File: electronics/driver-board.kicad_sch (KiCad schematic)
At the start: 65 parts, among them J1 Conn_01x02, J3 Motor_Conn_01x04, J5 Conn_01x06_Female, SW1 SW_Push, SW2 SW_Push, U2 LMR16020PDDAR, U3 ESP32-C6-MINI-1/U, U4 AMS1117-3.3, U5 TMC5240-TSSOP38, U6 MT6835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

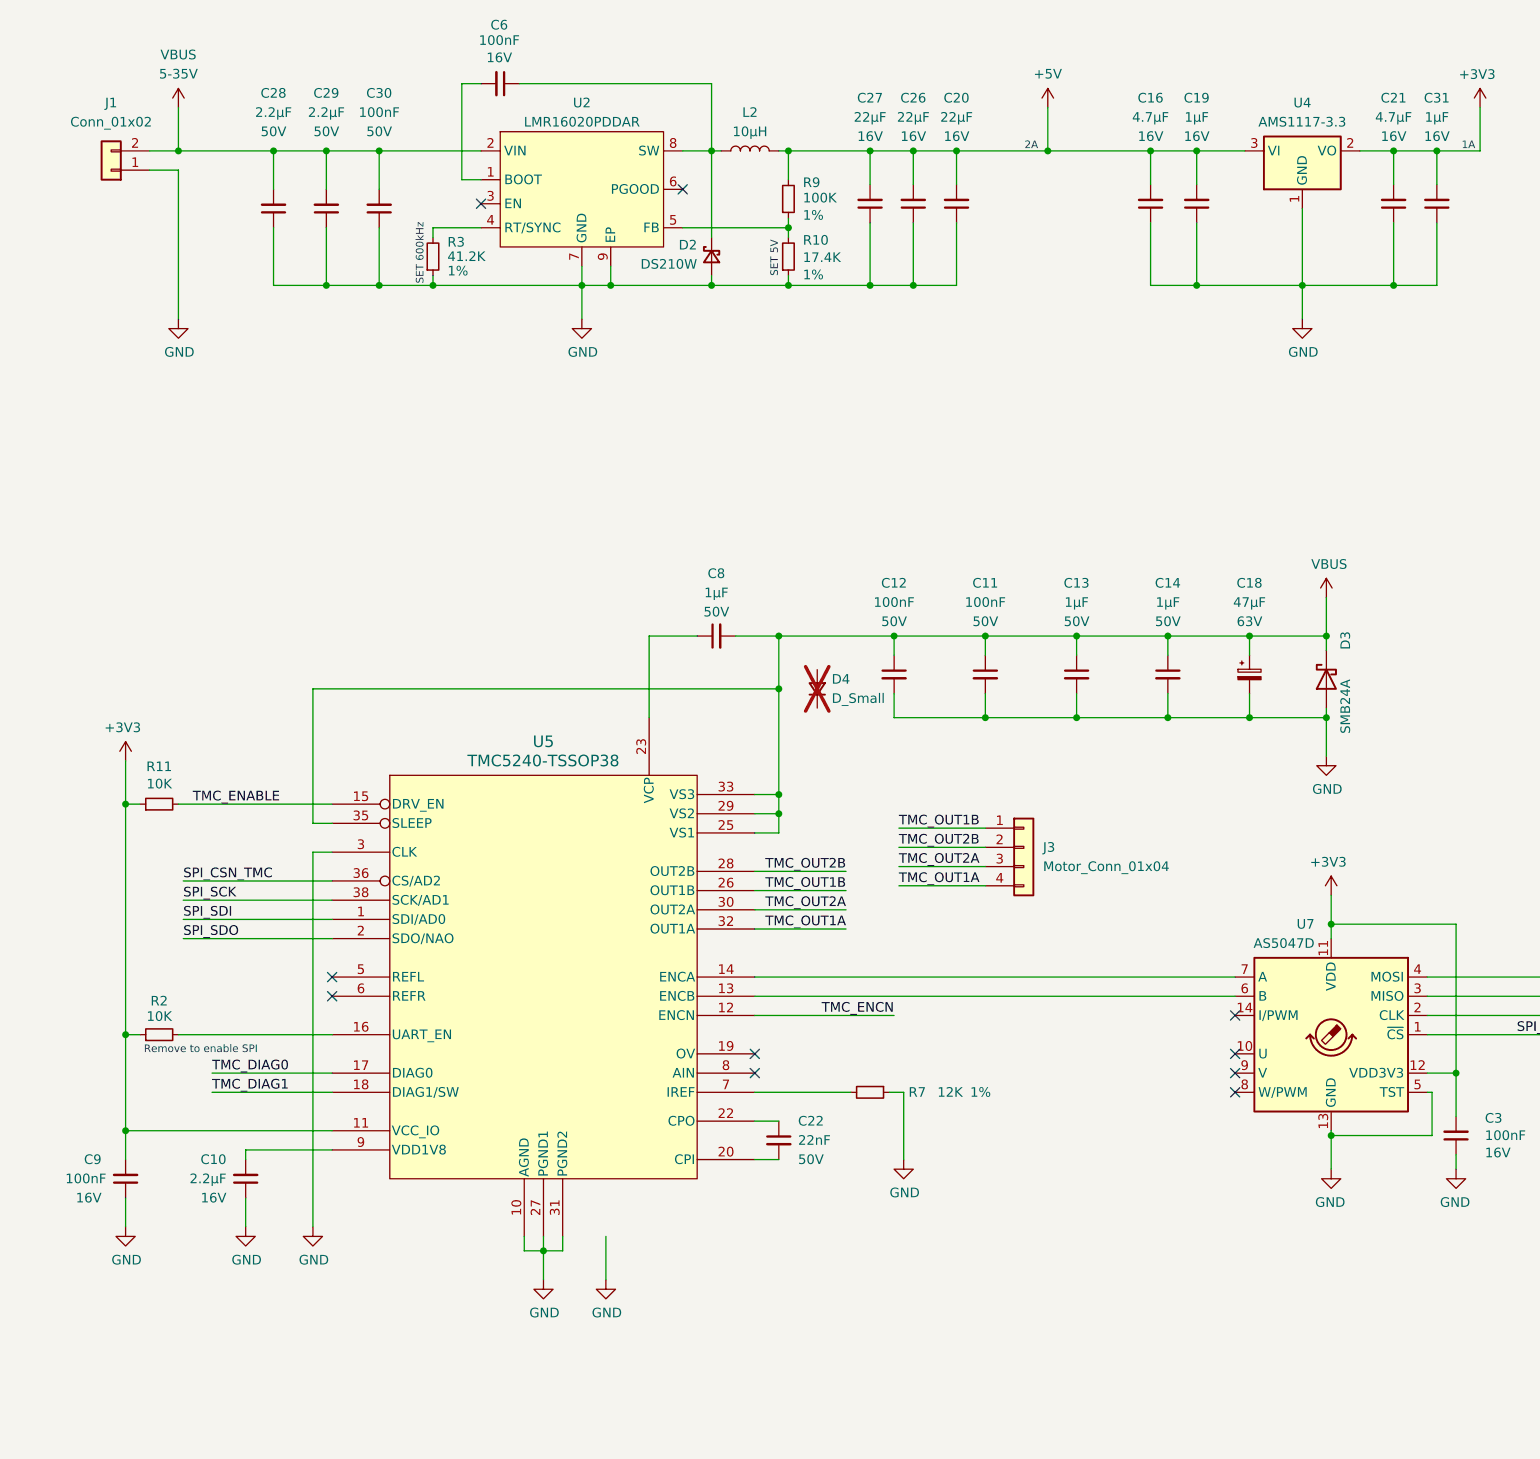
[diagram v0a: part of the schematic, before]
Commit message: splitted power cap into two and changed connector to wago
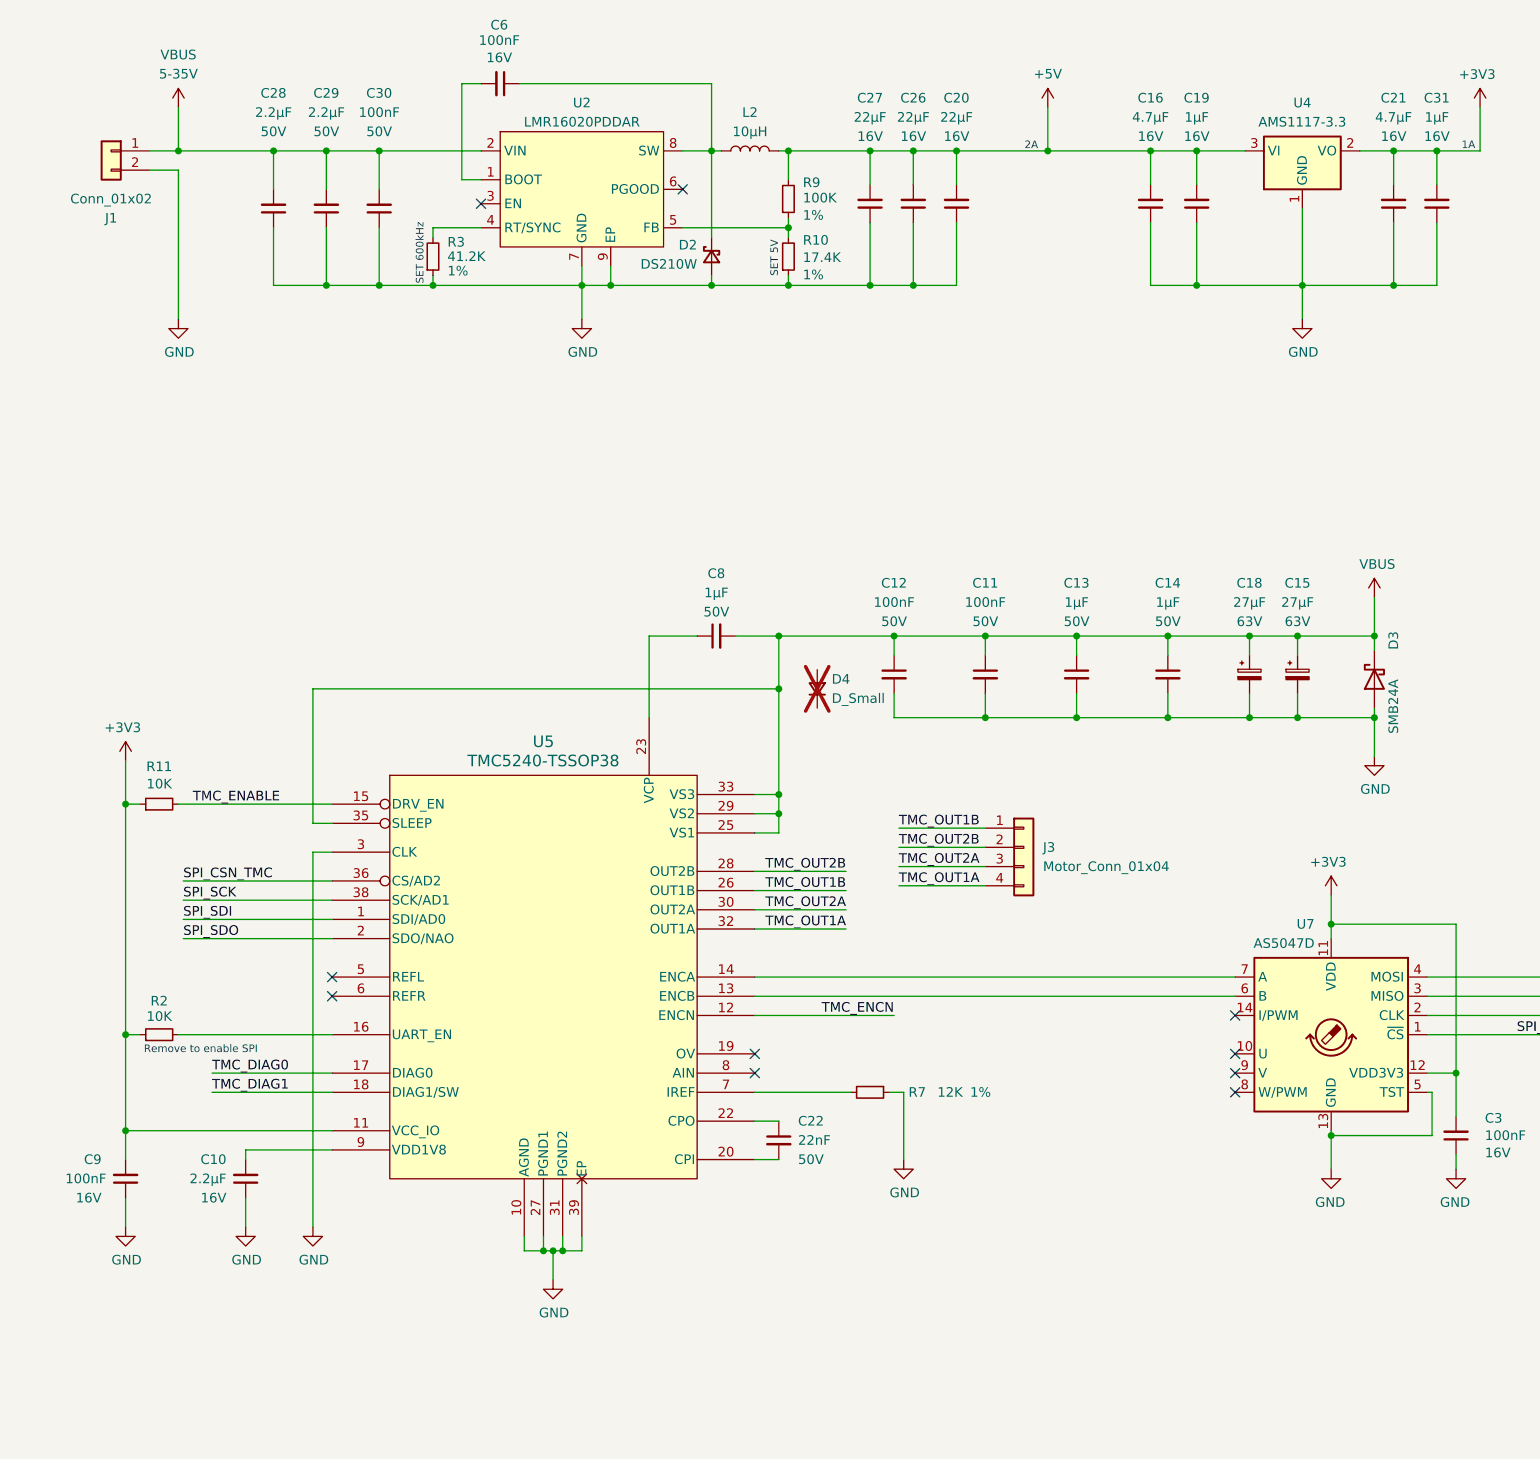
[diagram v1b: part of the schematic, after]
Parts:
- added C15: 27µF, Capacitor_SMD:CP_Elec_5x5.9, symbol Device:C_Polarized_Small
- C1, C17, C3, C4, C6, C9: LCSC (none) -> C66501; Manf# (none) -> CL10B104KO8NNNC; lcsc_part_number C66501 -> (none); mfr_part_number CL10B104KO8NNNC -> (none)
- C10: LCSC (none) -> C23630; Manf# (none) -> CL10A225KO8NNNC; lcsc_part_number C23630 -> (none); mfr_part_number CL10A225KO8NNNC -> (none)
- C11, C12, C30: LCSC (none) -> C1591; Manf# (none) -> CL10B104KB8NNNC; lcsc_part_number C1591 -> (none); mfr_part_number CL10B104KB8NNNC -> (none)
- C13, C14, C8: LCSC (none) -> C15849; Manf# (none) -> CL10A105KB8NNNC; lcsc_part_number C15849 -> (none); mfr_part_number CL10A105KB8NNNC -> (none)
- C16, C21: LCSC (none) -> C19666; Manf# (none) -> CL10A475KO8NNNC; lcsc_part_number C19666 -> (none); mfr_part_number CL10A475KO8NNNC -> (none)
- C18: value 47µF -> 27µF; LCSC (none) -> C487378; Manf (none) -> Ymin; Manf# (none) -> VKMB1001J270MV
- C19, C2, C31, C7: LCSC (none) -> C1592; Manf# (none) -> CL10A105KO8NNNC; lcsc_part_number C1592 -> (none); mfr_part_number CL10A105KO8NNNC -> (none)
- C20, C26, C27: LCSC (none) -> C2762594; Manf# (none) -> CL10A226MO7JZNC; lcsc_part_number C2762594 -> (none); mfr_part_number CL10A226MO7JZNC -> (none)
- C22: LCSC (none) -> C21122; Manf# (none) -> CL10B223KB8NNNC; lcsc_part_number C21122 -> (none); mfr_part_number CL10B223KB8NNNC -> (none)
- C28, C29: LCSC (none) -> C913904; Manf# (none) -> CL10A225KB8NNNC; lcsc_part_number C913904 -> (none); mfr_part_number CL10A225KB8NNNC -> (none)
- C5: LCSC (none) -> C92487; Manf# (none) -> CL10A106MO8NQNC; lcsc_part_number C92487 -> (none); mfr_part_number CL10A106MO8NQNC -> (none)
- D1: LCSC (none) -> C965555; Manf (none) -> Worldsemi; Manf# (none) -> WS2812B-2020; lcsc_part_number C965555 -> (none); mfr_part_number WS2812B-2020 -> (none)
- D2: LCSC (none) -> C116100; Manf (none) -> shikues; Manf# (none) -> DS210W; lcsc_part_number C116100 -> (none); mfr_part_number DS210W -> (none)
- D3: footprint Diode_SMD:D_1210_3225Metric -> Diode_SMD:D_SMB; DigiKey (none) -> F11623TR-ND; LCSC (none) -> C1975909; Manf (none) -> Littelfuse; Manf# (none) -> SZP6SMB24AT3G; digikey_part_number 2156-P6SMB24AT3G-ND -> (none); mfr_part_number P6SMB24AT3G -> (none)
- J1: footprint Connector_TE-Connectivity:TE_2834006-2_1x02_P4.0mm_Horizontal -> Slimc_Connector_Wago:2060-472&slash_998-404; LCSC (none) -> C3310225; Manf (none) -> Wago; Manf# (none) -> 2060-472/998-404; lcsc_part_number C86483 -> (none); mfr_part_number 2834006-2 -> (none)
- J3: DigiKey (none) -> 455-2243-ND; LCSC (none) -> C157925; Manf (none) -> JST; Manf# (none) -> S4B-XH-A; digikey_part_number 455-2243-ND -> (none); lcsc_part_number C157925 -> (none); mfr_part_number S4B-XH-A -> (none)
- L2: LCSC (none) -> C844996; Manf# (none) -> IHLP2020CZER100M01; lcsc_part_number C844996 -> (none); mfr_part_number IHLP2020CZER100M01 -> (none)
- R1, R11, R2, R4: LCSC (none) -> C4226066; Manf# (none) -> RT0603FRE1310KL; lcsc_part_number C4226066 -> (none); mfr_part_number RT0603FRE1310KL -> (none)
- R10: LCSC (none) -> C863611; Manf# (none) -> RT0603FRE0717K4L; lcsc_part_number C863611 -> (none); mfr_part_number RT0603FRE0717K4L -> (none)
- R3: LCSC (none) -> C706173; Manf# (none) -> RT0603FRE0741K2L; lcsc_part_number C706173 -> (none); mfr_part_number RT0603FRE0741K2L -> (none)
- R7: LCSC (none) -> C136933; Manf# (none) -> RT0603FRE0712KL; lcsc_part_number C136933 -> (none); mfr_part_number RT0603FRE0712KL -> (none)
- R9: LCSC (none) -> C728638; Manf# (none) -> RT0603FRE07100KL; lcsc_part_number C728638 -> (none); mfr_part_number RT0603FRE07100KL -> (none)
- SW1, SW2: LCSC (none) -> C231329; Manf (none) -> Omron Electronics; Manf# (none) -> B3U-1000P; lcsc_part_number C231329 -> (none); mfr_part_number B3U-1000P -> (none)
- U2: LCSC (none) -> C190006; Manf (none) -> Texas Instruments; Manf# (none) -> LMR16020PDDAR; lcsc_part_number C190006 -> (none); mfr_part_number LMR16020PDDAR -> (none)
- U3: LCSC (none) -> C5736265; Manf (none) -> Espressif; Manf# (none) -> ESP32-C6-MINI-1-N4; lcsc_part_number C5736265 -> (none); mfr_part_number ESP32-C6-MINI-1-N4 -> (none)
- U4: LCSC (none) -> C6186; Manf (none) -> Advanced Monolithic Systems; Manf# (none) -> AMS1117-3.3; lcsc_part_number C5181460 -> (none); mfr_part_number AMS1117-3.3 -> (none)
- U5: LCSC (none) -> SOP38-1EP; Manf (none) -> ADI Trinamic; Manf# (none) -> TMC5240AUU+; lcsc_part_number SOP38-1EP -> (none); mfr_part_number TMC5240AUU+ -> (none)
- U6: LCSC (none) -> C2932578; Manf# (none) -> MT6835GT-STD; lcsc_part_number C2932578 -> (none); mfr_part_number MT6835GT-STD -> (none)
- U7: LCSC (none) -> C962063; Manf (none) -> ams OSRAM; Manf# (none) -> AS5047P-ATSM; lcsc_part_number C962063 -> (none); mfr_part_number AS5047P-ATSM -> (none)
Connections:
- net GND: now also J1.2 (Pin_2), U5.39 (EP), C15.2; no longer J1.1 (Pin_1)
- net VBUS: now also J1.1 (Pin_1), C15.1; no longer J1.2 (Pin_2)
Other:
- moved on the sheet: D3, J1

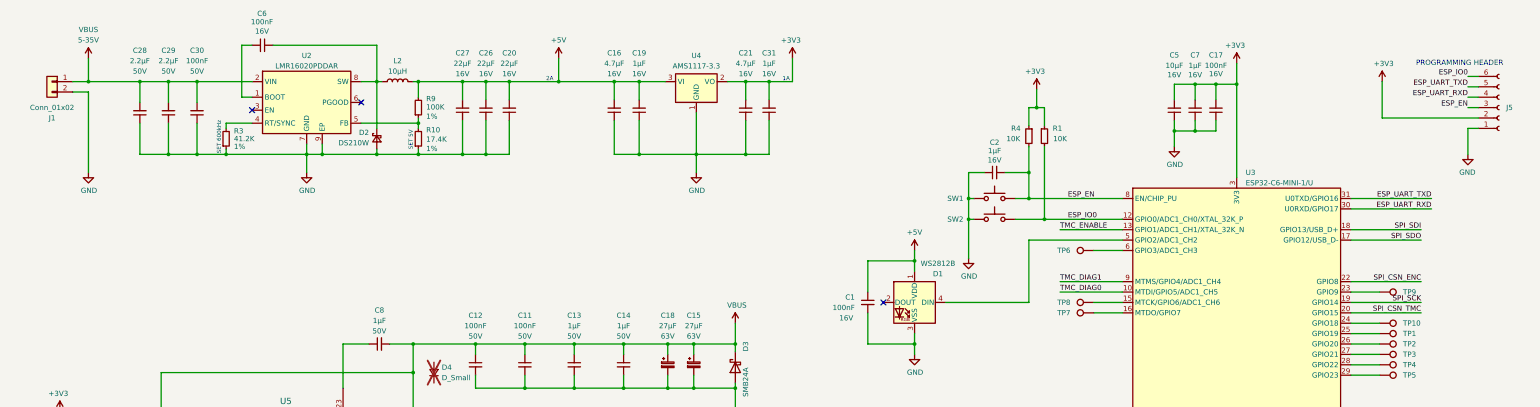
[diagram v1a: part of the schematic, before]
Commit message: fixed tmc5240 fp and esp32 boot pins
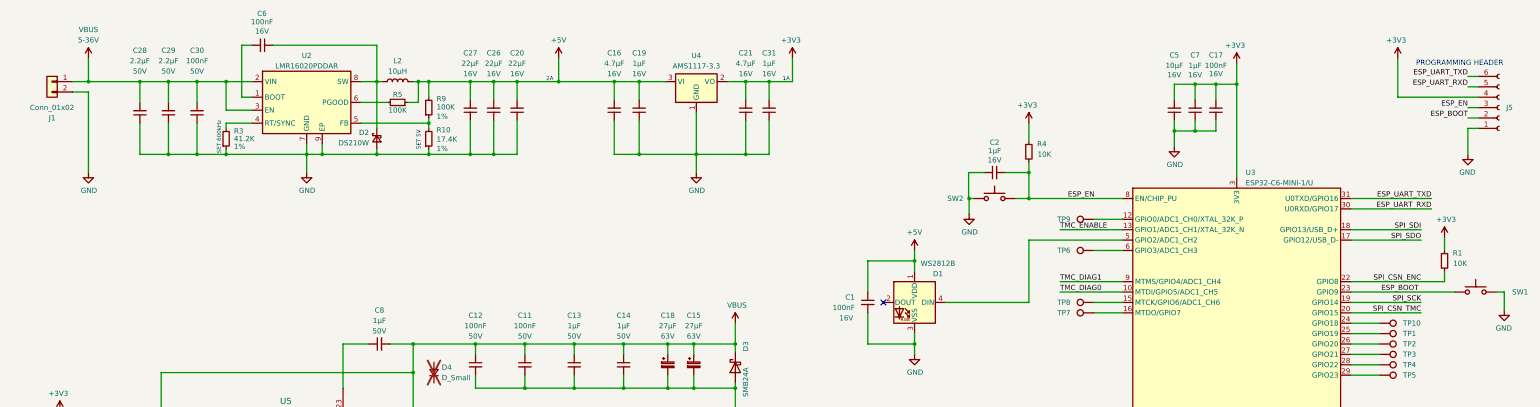
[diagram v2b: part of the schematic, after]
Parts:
- added R5: 100K, Resistor_SMD:R_0603_1608Metric, symbol Device:R_Small
- U5: footprint Package_SO:HTSSOP-38-1EP_6.1x12.5mm_P0.65mm_EP5.2x12.5mm_Mask3.39x6.35mm_ThermalVias -> Slimc_Package_SO:TSSOP-38_4.4x9.7mm_P0.5mm
- renumbered SW2 to SW1, SW1 to SW2
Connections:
- net +3V3: now also J5.4 (Pin_4); no longer J5.2 (Pin_2)
- net +5V: now also R5.1
- net ESP_UART_RXD: now also J5.5 (Pin_5); no longer J5.4 (Pin_4)
- net ESP_UART_TXD: now also J5.6 (Pin_6); no longer J5.5 (Pin_5)
- net SPI_CSN_ENC: now also R1.2
- net VBUS: now also U2.3 (EN)
- net at U2.6 (PGOOD): now also R5.2
- net at TP9.1: now also U3.12 (GPIO0/ADC1_CH0/XTAL_32K_P); no longer U3.23 (GPIO9)
- removed net ESP_IO0: J5.6 (Pin_6), R1.2, SW1.2, U3.12 (GPIO0/ADC1_CH0/XTAL_32K_P)
- new net ESP_BOOT: J5.2 (Pin_2), SW1.2, U3.23 (GPIO9)
- no-connect marks 18 -> 16
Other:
- moved on the sheet: C20, C26, C27, R1, R10, R4, R9, SW1
